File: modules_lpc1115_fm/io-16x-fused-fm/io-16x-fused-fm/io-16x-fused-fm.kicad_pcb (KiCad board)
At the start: 2 copper layers, 46.8 x 48.9 mm, 143 parts, among them IC5 LPC1115, IC6 ATAES132A-SHEQ-T, J1 62000611622, J2 1771017, J3 1770953, Q3 ASFL, U3 EEPROM, X1 MICROMATCH-10SMD

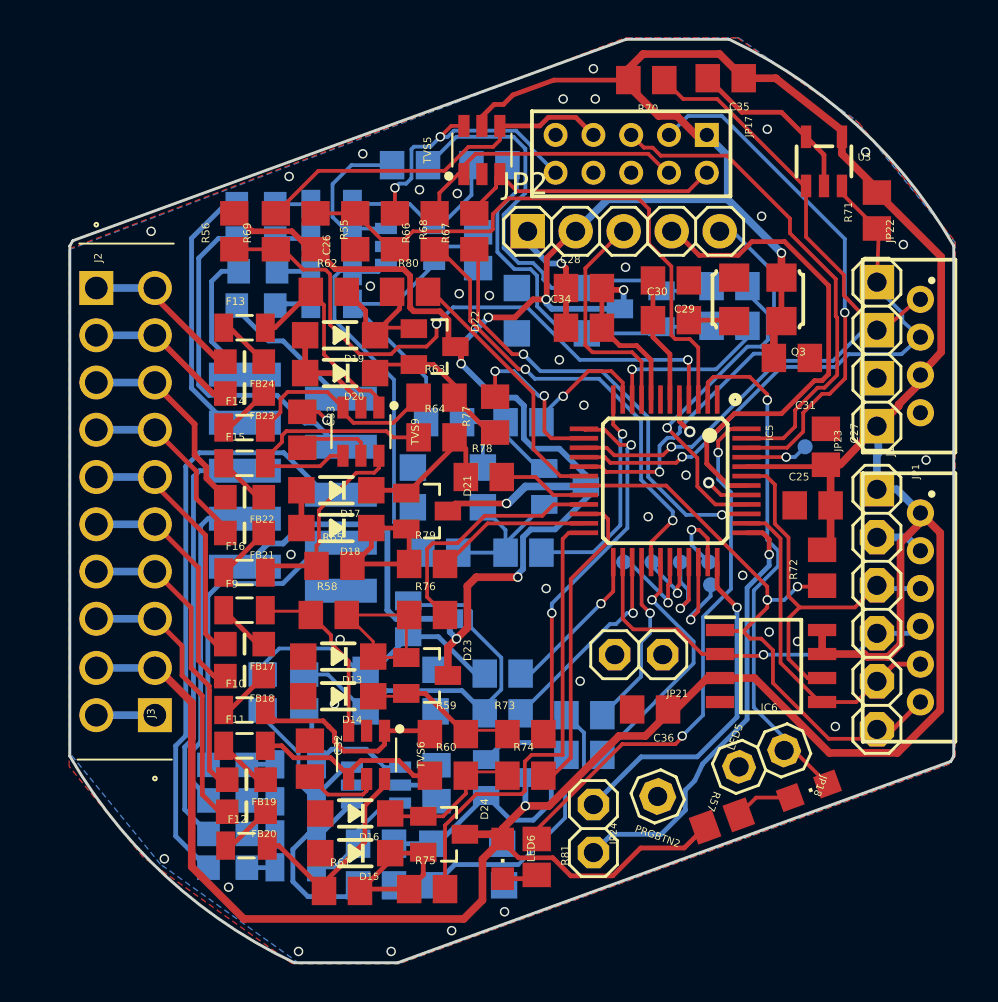
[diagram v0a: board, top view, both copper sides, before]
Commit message: bump io-16x-fused-fm - conversion mostly done
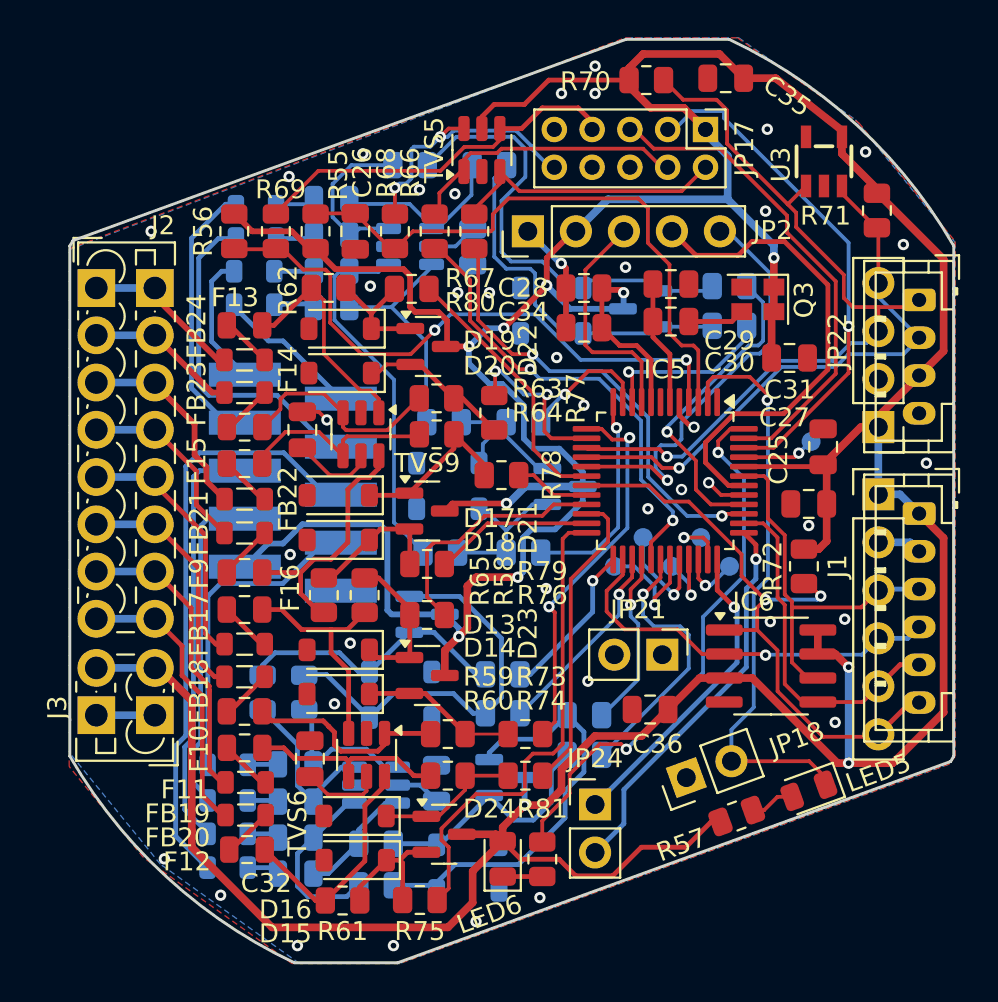
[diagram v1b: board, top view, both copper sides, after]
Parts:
- removed PRGBTN2: , io-16x-fused-fm:1X01
- C1, C2, C25, C26, C27, C28, C29, C30, C31, C32, C33, C34, C35, C36: footprint io-16x-fused-fm:C0805_334 -> Capacitor_SMD:C_0805_2012Metric
- D1, D13, D14, D15, D16, D17, D18, D19, D2, D20, D3, D4, D5, D6, D7, D8: footprint io-16x-fused-fm:SOD-123 -> Diode_SMD:D_SOD-123
- D10, D11, D12, D21, D22, D23, D24, D9: footprint io-16x-fused-fm:SOT23_210 -> Package_TO_SOT_SMD:SOT-23
- F1, F10, F11, F12, F13, F14, F15, F16, F2, F3, F4, F5, F6, F7, F8, F9: value BSMD0805-005-33V -> ?0805L; footprint io-16x-fused-fm:0805L -> Fuse:Fuse_0805_2012Metric
- FB1, FB17, FB18, FB19, FB2, FB20, FB21, FB22, FB23, FB24, FB3, FB4, FB5, FB6, FB7, FB8: footprint io-16x-fused-fm:FERR_0805MP -> Inductor_SMD:L_0805_2012Metric
- IC5: value LPC1115 -> LPC1115FBD48-303; footprint io-16x-fused-fm:LQFP48 -> Package_QFP:LQFP-48_7x7mm_P0.5mm
- IC6: footprint io-16x-fused-fm:SOIC127P600X175-8N -> Package_SO:SOIC-8_3.9x4.9mm_P1.27mm
- J1: value 62000611622 -> Conn_01x06; footprint io-16x-fused-fm:62000611622_15818693 -> Connector_JST:JST_PH_B6B-PH-K_1x06_P2.00mm_Vertical
- J2: footprint io-16x-fused-fm:1771017_40006276 -> TerminalBlock_Phoenix:TerminalBlock_Phoenix_PTSM-0,5-8-2.5-V-THR_1x08_P2.50mm_Vertical
- J3: footprint io-16x-fused-fm:1770953_40006276 -> TerminalBlock_Phoenix:TerminalBlock_Phoenix_PTSM-0,5-2-2.5-V-THR_1x02_P2.50mm_Vertical
- JP1: value (none) -> Conn_01x06_Pin; footprint io-16x-fused-fm:1X06-S -> Connector_PinHeader_2.54mm:PinHeader_1x06_P2.54mm_Vertical
- JP17: value J -> Conn_02x05_Odd_Even; footprint io-16x-fused-fm:2X05M -> Connector_PinHeader_2.00mm:PinHeader_2x05_P2.00mm_Vertical
- JP18, JP21, JP24: value (none) -> PINHD-1X2; footprint io-16x-fused-fm:1X02 -> Connector_PinHeader_2.54mm:PinHeader_1x02_P2.54mm_Vertical
- JP2: value (none) -> PINHD-1X5; footprint io-16x-fused-fm:1X05 -> Connector_PinHeader_2.54mm:PinHeader_1x05_P2.54mm_Vertical
- JP22: value 62000411622 -> Conn_01x04; footprint io-16x-fused-fm:62000411622 -> Connector_JST:JST_PH_B4B-PH-K_1x04_P2.00mm_Vertical
- JP23: value (none) -> Conn_01x04_Pin; footprint io-16x-fused-fm:1X04 -> Connector_PinHeader_2.54mm:PinHeader_1x04_P2.54mm_Vertical
- LED5: footprint io-16x-fused-fm:CHIPLED_0805_259 -> LED_SMD:LED_0805_2012Metric
- LED6: value (none) -> LEDCHIPLED_0805; footprint io-16x-fused-fm:CHIPLED_0805_259 -> LED_SMD:LED_0805_2012Metric
- Q3: value ASFL -> 12 MHz; footprint io-16x-fused-fm:ASF_204 -> Oscillator:Oscillator_SMD_SeikoEpson_SG210-4Pin_2.5x2.0mm
- R1, R10, R11, R12, R13, R14, R15, R16, R2, R3, R4, R5, R55, R56, R57, R58, R59, R6, R60, R61, R62, R63, R64, R65, R66, R67, R68, R69, R7, R70, R71, R72, R73, R74, R75, R76, R77, R78, R79, R8, R80, R81, R9: footprint io-16x-fused-fm:R0805_334 -> Resistor_SMD:R_0805_2012Metric
- TP1, TP2, TP3, TP4, TP5, TP6: footprint io-16x-fused-fm:TP08R_385 -> TestPoint:TestPoint_Pad_D1.0mm
- TVS1, TVS2, TVS5, TVS6, TVS9: footprint io-16x-fused-fm:SOT-23-6L -> Package_TO_SOT_SMD:SOT-23-6
- moved JP1 6.08 mm to (167.9, 104.6), turned to 0 degrees
- moved JP2 5.07 mm to (149.4, 90.7), turned to 90 degrees
- moved J1 5.00 mm to (170.1, 105.7), turned to -90 degrees
- moved JP17 4.14 mm to (158.8, 85.3), turned to -90 degrees
- moved JP18 4.11 mm to (157.7, 119.6), turned to 110 degrees
- moved JP23 3.86 mm to (167.9, 101.1), turned to 180 degrees
- moved JP22 3.02 mm to (170.1, 94.4), turned to -90 degrees
- moved R58 2.17 mm to (140.7, 110.0), turned to 90 degrees
- moved R65 1.65 mm to (138.6, 110.0), turned to 90 degrees
- moved TP4 1.40 mm to (160.0, 108.5)
- moved TP2 1.38 mm to (155.4, 106.9)
- moved TP5 1.37 mm to (158.5, 106.9)
- moved JP24 1.28 mm to (152.9, 121.1), turned to 0 degrees
- moved JP21 1.25 mm to (156.5, 113.1), turned to -90 degrees
- moved R72 0.96 mm to (164.0, 108.5)
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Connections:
- net BUS_V renamed /BUS_V
- net DBG_RXD renamed /DBG_RXD
- net DBG_TXD renamed /DBG_TXD
- net EIB_IN renamed /EIB_IN
- net EIB_OUT renamed /EIB_OUT
- net IO1 renamed /IO1
- net IO10 renamed /IO10
- net IO11 renamed /IO11
- net IO12 renamed /IO12
- net IO13 renamed /IO13
- net IO14 renamed /IO14
- net IO15 renamed /IO15
- net IO16 renamed /IO16
- net IO2 renamed /IO2
- net IO3 renamed /IO3
- net IO4 renamed /IO4
- net IO5 renamed /IO5
- net IO6 renamed /IO6
- net IO7 renamed /IO7
- net IO8 renamed /IO8
- net IO9 renamed /IO9
- net ISP_EN renamed /ISP_EN
- net ISP_RXD renamed /ISP_RXD
- net ISP_TXD renamed /ISP_TXD
- net MISO1 renamed /MISO1
- net MOSI1 renamed /MOSI1
- net N$10 renamed /N$10
- net N$11 renamed /N$11
- net N$12 renamed /N$12
- net N$13 renamed /N$13
- net N$14 renamed /N$14
- net N$15 renamed /N$15
- net N$16 renamed /N$16
- net N$17 renamed /N$17
- net N$2 renamed /N$2
- net N$22 renamed /N$22
- net N$3 renamed /N$3
- net N$4 renamed /N$4
- net N$5 renamed /N$5
- net RESET renamed /RESET
- net SCK1 renamed /SCK1
- net SCL renamed /SCL
- net SDA renamed /SDA
- net SSEL1 renamed /SSEL1
- net SWCLK renamed /SWCLK
- net SWDIO renamed /SWDIO
- net SWD_ISP_EN renamed /SWD_ISP_EN
- net SWD_RESET renamed /SWD_RESET
- net SWD_SWCLK renamed /SWD_SWCLK
- net SWD_SWDIO renamed /SWD_SWDIO
- net XTALIN renamed /XTALIN
- net XTAL_EN renamed /XTAL_EN
- D10 pad 1: N$56 -> Net-(D2-K)
- D10 pad 2: N$55 -> Net-(D1-K)
- D11 pad 1: N$44 -> Net-(D5-K)
- D11 pad 2: N$43 -> Net-(D6-K)
- D12 pad 1: N$18 -> Net-(D8-K)
- D12 pad 2: N$19 -> Net-(D7-K)
- D21 pad 1: IO3R -> /IO3R
- D21 pad 2: IO4R -> /IO4R
- D22 pad 1: IO1R -> /IO1R
- D22 pad 2: IO2R -> /IO2R
- D23 pad 1: IO5R -> /IO5R
- D23 pad 2: IO6R -> /IO6R
- D24 pad 1: IO7R -> /IO7R
- D24 pad 2: IO8R -> /IO8R
- D9 pad 1: N$57 -> Net-(D3-K)
- D9 pad 2: N$58 -> Net-(D4-K)
- FB17 pad 2: IN5 -> /IN5
- FB18 pad 2: IN6 -> /IN6
- FB19 pad 2: IN7 -> /IN7
- FB20 pad 2: IN8 -> /IN8
- FB21 pad 2: IN4 -> /IN4
- FB22 pad 2: IN3 -> /IN3
- FB23 pad 2: IN2 -> /IN2
- FB24 pad 2: IN1 -> /IN1
- IC5 pad 2: PROG -> /PROG
- IC5 pad 31: N$62 -> Net-(IC5-PIO2_11)
- IC5 pad 32: N$27 -> Net-(IC5-PIO0_11)
- IC5 pad 33: N$46 -> Net-(IC5-PIO1_0)
- IC5 pad 34: N$60 -> Net-(IC5-PIO1_1)
- IC5 pad 35: N$61 -> Net-(IC5-PIO1_2)
- IC5 pad 45: N$20 -> Net-(IC5-PIO1_5)
- IC5 pad 7: (no net) -> unconnected-(IC5-XTALOUT-Pad7)
- J2 pad 1: IN1 -> /IN1
- J2 pad 2: IN1 -> /IN2
- J2 pad 3: IN2 -> /IN3
- J2 pad 4: IN2 -> /IN4
- J2 pad 5: IN3 -> /IN5
- J2 pad 6: IN3 -> /IN6
- J2 pad 7: IN4 -> /IN7
- J2 pad 8: IN4 -> /IN8
- J3 pad 2: GND -> +3V3
- JP17 pad 6: (no net) -> unconnected-(JP17-Pin_6-Pad6)
- JP17 pad 8: (no net) -> unconnected-(JP17-Pin_8-Pad8)
- JP18 pad 1: PROG -> GND
- JP18 pad 2: GND -> /PROG
- JP21 pad 1: (no net) -> unconnected-(JP21-Pin_1-Pad1)
- JP21 pad 2: (no net) -> unconnected-(JP21-Pin_2-Pad2)
- R1 pad 2: N$55 -> Net-(D1-K)
- R10 pad 1: N$57 -> Net-(D3-K)
- R11 pad 1: N$58 -> Net-(D4-K)
- R12 pad 1: N$55 -> Net-(D1-K)
- R13 pad 1: N$19 -> Net-(D7-K)
- R14 pad 1: N$43 -> Net-(D6-K)
- R15 pad 1: N$44 -> Net-(D5-K)
- R16 pad 1: N$18 -> Net-(D8-K)
- R2 pad 2: N$56 -> Net-(D2-K)
- R3 pad 2: N$57 -> Net-(D3-K)
- R4 pad 2: N$58 -> Net-(D4-K)
- R5 pad 2: N$18 -> Net-(D8-K)
- R57 pad 1: N$26 -> Net-(LED5-A)
- R58 pad 2: IO5R -> /IO5R
- R59 pad 2: IO6R -> /IO6R
- R6 pad 2: N$19 -> Net-(D7-K)
- R60 pad 2: IO7R -> /IO7R
- R61 pad 2: IO8R -> /IO8R
- R62 pad 2: IO1R -> /IO1R
- R63 pad 2: IO2R -> /IO2R
- R64 pad 2: IO3R -> /IO3R
- R65 pad 2: IO4R -> /IO4R
- R7 pad 2: N$43 -> Net-(D6-K)
- R73 pad 1: IO6R -> /IO6R
- R74 pad 1: IO7R -> /IO7R
- R75 pad 1: IO8R -> /IO8R
- R76 pad 1: IO5R -> /IO5R
- R77 pad 1: IO2R -> /IO2R
- R78 pad 1: IO3R -> /IO3R
- R79 pad 1: IO4R -> /IO4R
- R8 pad 2: N$44 -> Net-(D5-K)
- R80 pad 1: IO1R -> /IO1R
- R81 pad 2: N$38 -> Net-(LED6-K)
- R9 pad 1: N$56 -> Net-(D2-K)
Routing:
- net /PROG: track 0.00 -> 30.6 mm, vias 0 -> 1
- net PROG: track 27.9 -> 0.00 mm, vias 1 -> 0
- net Net-(D8-K): track 0.00 -> 24.5 mm
- net N$18: track 24.3 -> 0.00 mm
- net Net-(D4-K): track 0.00 -> 22.1 mm
- net N$58: track 22.0 -> 0.00 mm
- net Net-(D1-K): track 0.00 -> 21.6 mm
- net N$55: track 21.3 -> 0.00 mm
- net N$19: track 19.5 -> 0.00 mm
- net Net-(D7-K): track 0.00 -> 19.5 mm
- net GND: track 35.1 -> 16.8 mm
- net IN7: track 16.0 -> 0.00 mm
- net /IN7: track 0.00 -> 15.9 mm
- net /IN8: track 0.00 -> 15.1 mm
- net IN8: track 15.1 -> 0.00 mm
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
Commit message: io-16x-fused-fm: use micro-match from selfbus library
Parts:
- JP1: footprint Connector_PinHeader_2.54mm:PinHeader_1x06_P2.54mm_Vertical -> selfbus:PinHeader_1x06_P2.54mm_Vertical_no_silkscreen
- JP23: footprint Connector_PinHeader_2.54mm:PinHeader_1x04_P2.54mm_Vertical -> selfbus:PinHeader_1x04_P2.54mm_Vertical_no_silkscreen
- U3: footprint io-16x-fused-fm:SOT23-5 -> Package_TO_SOT_SMD:SOT-23-5
- X1: footprint io-16x-fused-fm:MICROMATCH-10SMD -> selfbus:TE_Connectivity_MICRO-MATCH_SMD_FTE_1-188275-0_2x05_P1.27mm_Vertical
- moved U3 0.38 mm to (164.8, 87.4), turned to 90 degrees
- moved D19 0.28 mm to (139.7, 95.9)
- moved D20 0.28 mm to (139.7, 98.2)
- moved D17 0.25 mm to (139.6, 104.7)
- moved D18 0.25 mm to (139.6, 107.1)
- turned X1 to 90 degrees
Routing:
- net GND: vias 40 -> 41

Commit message: finally standardize selected parts on all boards
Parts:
- C1, C2, C27, C32, C33, C34, C35, C36: value 100nF -> 100n
- C25, C28: value 1uF -> 1u
- C26, C31: value 10nF -> 10n
- C29: value 220pF -> 220p
- C30: value 100pF -> 100p
- F1, F10, F11, F12, F13, F14, F15, F16, F2, F3, F4, F5, F6, F7, F8, F9: value ?0805L -> BSMD0805-005-33V
- Q3: value 12 MHz -> 12MHz
- R70, R71: value 3,3k -> 3k3

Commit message: final for manufacturing
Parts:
- R10, R11, R12, R13, R14, R15, R16, R73, R74, R75, R76, R77, R78, R79, R80, R9: value 100R -> 100
- U3: value EEPROM -> MCP24AA32 EEPROM
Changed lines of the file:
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@@
 			)
 		)
-		(property "Value" "100R"
+		(property "Value" "100"
 			(at 0 1.65 0)
 			(layer "F.Fab")
@@
 			)
 		)
-		(property "Value" "100R"
+		(property "Value" "100"
 			(at 0 1.65 0)
 			(layer "F.Fab")
@@
 			)
 		)
-		(property "Value" "100R"
+		(property "Value" "100"
 			(at 0 1.65 0)
 			(layer "F.Fab")
@@
 			)
 		)
-		(property "Value" "EEPROM"
+		(property "Value" "MCP24AA32 EEPROM"
 			(at 0 2.4 90)
 			(layer "F.Fab")
@@
 			)
 		)
-		(property "Datasheet" ""
+		(property "Datasheet" "http://ww1.microchip.com/downloads/en/DeviceDoc/21709J.pdf"
 			(at 0 0 90)
 			(unlocked yes)
@@
 			)
 		)
-		(property "Description" ""
+		(property "Description" "I2C Serial EEPROM, 2Kb, SOT-23"
 			(at 0 0 90)
 			(unlocked yes)
@@
 			)
 		)
+		(property ki_fp_filters "SOT?23*")
 		(sheetname "Stammblatt")
 		(sheetfile "io-16x-fused-fm.kicad_sch")
@@
 			(net 87 "/SCL")
 			(pinfunction "SCL")
-			(pintype "bidirectional")
+			(pintype "input")
 		)
 		(pad "2" smd roundrect
@@
 			(roundrect_rratio 0.25)
 			(net 1 "GND")
-			(pinfunction "GND")
-			(pintype "bidirectional")
+			(pinfunction "V_{SS}")
+			(pintype "power_in")
 		)
 		(pad "3" smd roundrect
@@
 			(roundrect_rratio 0.25)
 			(net 2 "+3V3")
-			(pinfunction "VCC")
-			(pintype "bidirectional")
+			(pinfunction "V_{CC}")
+			(pintype "power_in")
 		)
 		(pad "5" smd roundrect
@@
 			(net 1 "GND")
 			(pinfunction "WP")
-			(pintype "bidirectional")
+			(pintype "input")
 		)
 		(model "${KICAD8_3DMODEL_DIR}/Package_TO_SOT_SMD.3dshapes/SOT-23-5.wrl"
@@
 			)
 		)
-		(property "Value" "100R"
+		(property "Value" "100"
 			(at 0 1.65 0)
 			(layer "F.Fab")
@@
 			)
 		)
-		(property "Value" "100R"
+		(property "Value" "100"
 			(at 0 1.65 90)
 			(layer "F.Fab")
@@
 			)
 		)
-		(property "Value" "100R"
+		(property "Value" "100"
 			(at 0 1.65 0)
 			(layer "F.Fab")
@@
 			)
 		)
-		(property "Value" "100R"
+		(property "Value" "100"
 			(at 0 1.65 0)
 			(layer "F.Fab")
@@
 			)
 		)
-		(property "Value" "100R"
+		(property "Value" "100"
 			(at 0 1.65 0)
 			(layer "F.Fab")
@@
 			)
 		)
-		(property "Value" "100R"
+		(property "Value" "100"
 			(at 0 -1.65 0)
 			(layer "B.Fab")
@@
 			)
 		)
-		(property "Value" "100R"
+		(property "Value" "100"
 			(at 0 -1.65 0)
 			(layer "B.Fab")
@@
 			)
 		)
-		(property "Value" "100R"
+		(property "Value" "100"
 			(at 0 -1.65 0)
 			(layer "B.Fab")
@@
 			)
 		)
-		(property "Value" "100R"
+		(property "Value" "100"
 			(at 0 -1.65 0)
 			(layer "B.Fab")
@@
 			)
 		)
-		(property "Value" "100R"
+		(property "Value" "100"
 			(at 0 -1.65 0)
 			(layer "B.Fab")
@@
 			)
 		)
-		(property "Value" "100R"
+		(property "Value" "100"
 			(at 0 -1.65 0)
 			(layer "B.Fab")
@@
 			)
 		)
-		(property "Value" "100R"
+		(property "Value" "100"
 			(at 0 -1.65 0)
 			(layer "B.Fab")
@@
 			)
 		)
-		(property "Value" "100R"
+		(property "Value" "100"
 			(at 0 -1.65 0)
 			(layer "B.Fab")

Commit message: update xtal caps, eib_in cap+resistor, bus_v resistors
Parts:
- C29: value 220p -> 22p
- C30: value 100p -> 22p
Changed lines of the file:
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@@
 		(sheetname "Stammblatt")
 		(sheetfile "io-16x-fused-fm.kicad_sch")
-		(attr smd)
+		(attr smd exclude_from_bom dnp)
 		(fp_line
 			(start -0.261252 0.735)
@@
 		(sheetname "Stammblatt")
 		(sheetfile "io-16x-fused-fm.kicad_sch")
-		(attr through_hole)
+		(attr through_hole exclude_from_bom dnp)
 		(fp_line
 			(start -1.33 -1.33)
@@
 		(sheetname "Stammblatt")
 		(sheetfile "io-16x-fused-fm.kicad_sch")
-		(attr smd)
+		(attr smd exclude_from_bom dnp)
 		(fp_line
 			(start 0 -1.56)
@@
 		(sheetname "Stammblatt")
 		(sheetfile "io-16x-fused-fm.kicad_sch")
-		(attr smd)
+		(attr smd exclude_from_bom dnp)
 		(fp_line
 			(start 0 -2.56)
@@
 			)
 		)
-		(property "Value" "100p"
+		(property "Value" "22p"
 			(at 0 1.68 0)
 			(layer "F.Fab")
@@
 		(sheetname "Stammblatt")
 		(sheetfile "io-16x-fused-fm.kicad_sch")
-		(attr smd)
+		(attr smd exclude_from_bom dnp)
 		(fp_line
 			(start -0.261252 0.735)
@@
 		(sheetname "Stammblatt")
 		(sheetfile "io-16x-fused-fm.kicad_sch")
-		(attr through_hole)
+		(attr through_hole exclude_from_bom dnp)
 		(fp_line
 			(start -1.33 -1.33)
@@
 			)
 		)
-		(property "Value" "220p"
+		(property "Value" "22p"
 			(at 0 1.68 180)
 			(layer "F.Fab")
